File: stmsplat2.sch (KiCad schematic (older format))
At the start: 98 parts, among them J1 C11_2X36, J10 Conn_01x03_Male, J11 Conn_01x02_Male, J12 Conn_01x04_Male, J13 Conn_01x04_Male, J14 Conn_01x02, J15 Conn_01x02, J16 Screw_Terminal_01x03, J17 Screw_Terminal_01x02, J2 C12_2X36, J3 Conn_01x04_Male, J4 Conn_01x04_Male, J5 Conn_Coaxial, J6 Conn_01x04_Male, J7 Conn_01x04_Male, J8 Conn_01x04_Male, J9 Conn_01x03_Male, Q1 BSS138LT1G, U1 ublox_chinese_PCB_module, U10 XCVR_E30-400M20S, U11 3115_module, U2 ESP-C3-13U, U3 SST25VF032B, U4 48L512-48LM01, U5 Opamp_Quad_MCP6024, U6 E180-ZG120A, U7 AZ1084C, U8 MCP6S93-X_UN, U9 DS2485

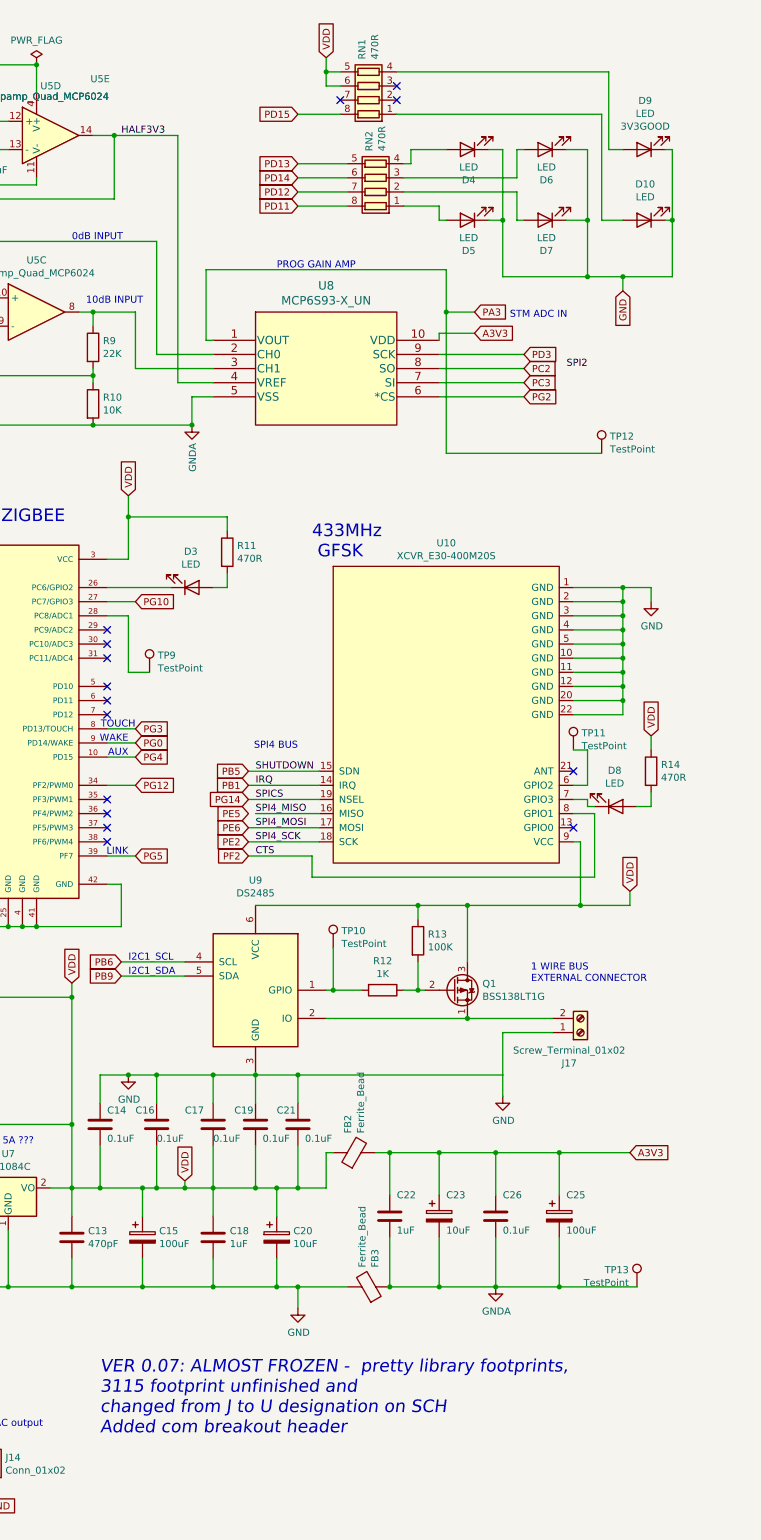
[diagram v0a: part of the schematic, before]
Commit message: Ver 0.9. Initial PCB placement attempt. Some footprints changed
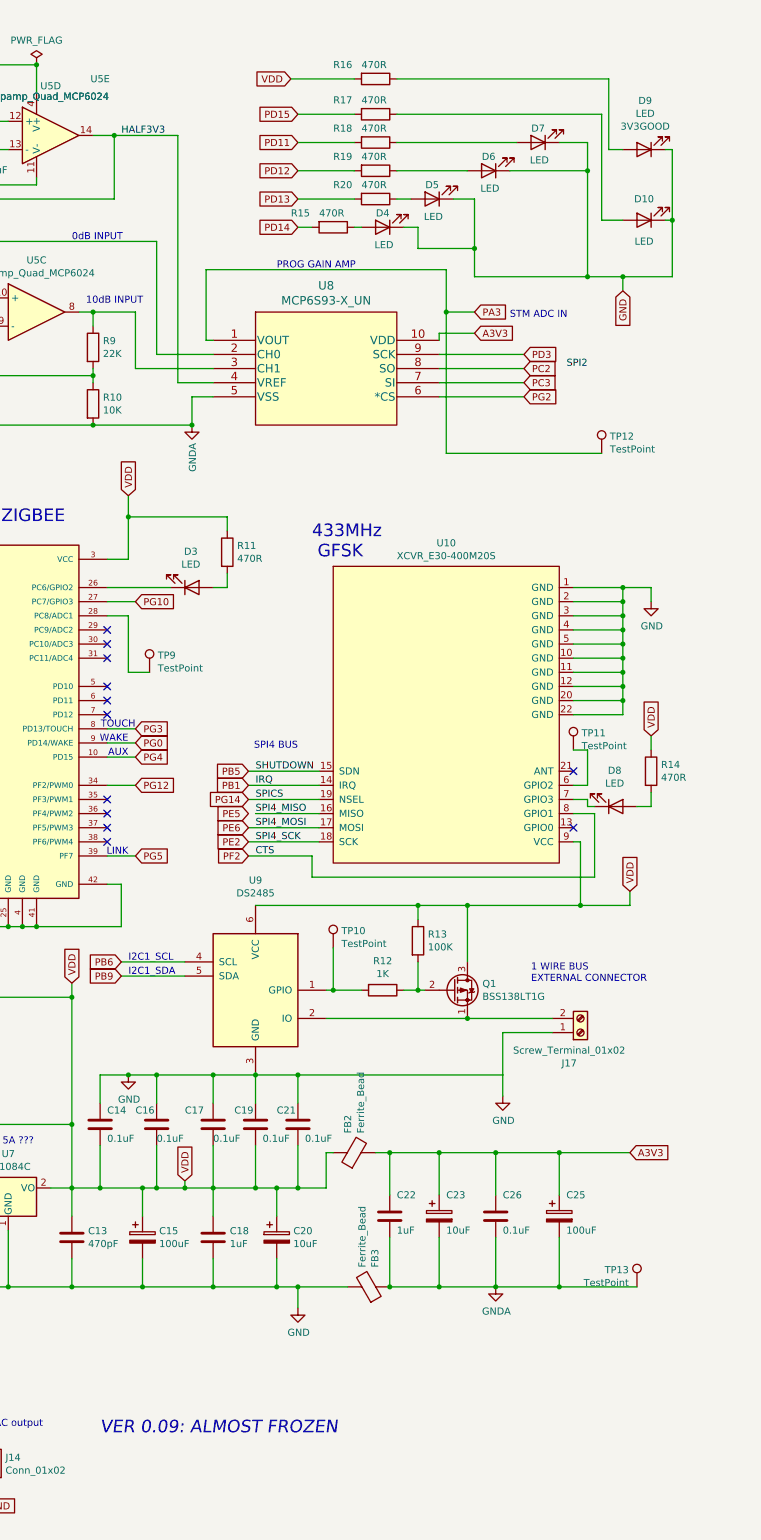
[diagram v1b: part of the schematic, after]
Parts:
- removed RN1, RN2: 470R, Resistor_SMD:R_Array_Convex_4x1206, symbol Device:R_Pack04
- added R15, R16, R17, R18, R19, R20: 470R, Resistor_SMD:R_0805_2012Metric, symbol Device:R
- U3: Alternate (none) -> SST25VF016B (only 2MByte)
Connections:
- net PD11: now also R18.2
- net PD12: now also R19.2
- net PD13: now also R20.2
- net PD14: now also R15.2
- net PD15: now also R17.2
- net VDD: now also R16.2
- net at D7.2 (A): now also R18.1
- net at D5.2 (A): now also R20.1
- net at D6.2 (A): now also R19.1
- net at D4.2 (A): now also R15.1
- net at D9.2 (A): now also R16.1
- net at D10.2 (A): now also R17.1
- no-connect marks 78 -> 75
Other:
- note added: "VER 0.09: ALMOST FROZEN \n"
- note removed: "VER 0.07: ALMOST FROZEN - pretty library footprints,\n3115 footprint unfinished and \nchanged from J to U designation on SCH\nAdded com breakout header"
- moved on the sheet: D4, D5, D6, D7
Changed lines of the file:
@@
 EESchema Schematic File Version 4
-LIBS:stmsplat2-cache
-EELAYER 26 0
+EELAYER 30 0
 EELAYER END
 $Descr A3 16535 11693
@@
 L Device:LED D7
 U 1 1 5BF5D97C
-P 15050 1900
-F 0 "D7" H 15041 2116 50  0000 C CNN
-F 1 "LED" H 15041 2025 50  0000 C CNN
-F 2 "LED_SMD:LED_PLCC-2" H 15050 1900 50  0001 C CNN
-F 3 "~" H 15050 1900 50  0001 C CNN
-	1    15050 1900
+P 15000 1350
+F 0 "D7" H 15000 1250 50  0000 C CNN
+F 1 "LED" H 14991 1475 50  0000 C CNN
+F 2 "LED_SMD:LED_PLCC-2" H 15000 1350 50  0001 C CNN
+F 3 "~" H 15000 1350 50  0001 C CNN
+	1    15000 1350
 	-1   0    0    1
 $EndComp
@@
 L Device:LED D5
 U 1 1 5BF5DD08
-P 14500 1900
-F 0 "D5" H 14491 2116 50  0000 C CNN
-F 1 "LED" H 14491 2025 50  0000 C CNN
-F 2 "LED_SMD:LED_PLCC-2" H 14500 1900 50  0001 C CNN
-F 3 "~" H 14500 1900 50  0001 C CNN
-	1    14500 1900
+P 14250 1750
+F 0 "D5" H 14250 1650 50  0000 C CNN
+F 1 "LED" H 14241 1875 50  0000 C CNN
+F 2 "LED_SMD:LED_PLCC-2" H 14250 1750 50  0001 C CNN
+F 3 "~" H 14250 1750 50  0001 C CNN
+	1    14250 1750
 	-1   0    0    1
 $EndComp
@@
 GND
 $Comp
-L Device:R_Pack04 RN2
-U 1 1 5BF93731
-P 13850 1600
-F 0 "RN2" H 14038 1646 50  0000 L CNN
-F 1 "470R" H 14038 1555 50  0000 L CNN
-F 2 "Resistor_SMD:R_Array_Convex_4x1206" V 14125 1600 50  0001 C CNN
-F 3 "" H 13850 1600 50  0001 C CNN
-	1    13850 1600
-	0    -1   -1   0
-$EndComp
-$Comp
 L Device:LED D6
 U 1 1 5BF93B87
-P 15050 1400
-F 0 "D6" H 15041 1616 50  0000 C CNN
-F 1 "LED" H 15041 1525 50  0000 C CNN
-F 2 "LED_SMD:LED_PLCC-2" H 15050 1400 50  0001 C CNN
-F 3 "~" H 15050 1400 50  0001 C CNN
-	1    15050 1400
+P 14650 1550
+F 0 "D6" H 14650 1450 50  0000 C CNN
+F 1 "LED" H 14641 1675 50  0000 C CNN
+F 2 "LED_SMD:LED_PLCC-2" H 14650 1550 50  0001 C CNN
+F 3 "~" H 14650 1550 50  0001 C CNN
+	1    14650 1550
 	-1   0    0    1
 $EndComp
@@
 L Device:LED D4
 U 1 1 5BF93B8D
-P 14500 1400
-F 0 "D4" H 14491 1616 50  0000 C CNN
-F 1 "LED" H 14491 1525 50  0000 C CNN
-F 2 "LED_SMD:LED_PLCC-2" H 14500 1400 50  0001 C CNN
-F 3 "~" H 14500 1400 50  0001 C CNN
-	1    14500 1400
+P 13900 1950
+F 0 "D4" H 13900 1850 50  0000 C CNN
+F 1 "LED" H 13891 2075 50  0000 C CNN
+F 2 "LED_SMD:LED_PLCC-2" H 13900 1950 50  0001 C CNN
+F 3 "~" H 13900 1950 50  0001 C CNN
+	1    13900 1950
 	-1   0    0    1
 $EndComp
 $Comp
-L Device:R_Pack04 RN1
-U 1 1 5BFA3139
-P 13800 950
-F 0 "RN1" H 13988 996 50  0000 L CNN
-F 1 "470R" H 13988 905 50  0000 L CNN
-F 2 "Resistor_SMD:R_Array_Convex_4x1206" V 14075 950 50  0001 C CNN
-F 3 "" H 13800 950 50  0001 C CNN
-	1    13800 950
-	0    -1   -1   0
-$EndComp
-$Comp
 L Device:LED D10
 U 1 1 5BFA313F
 P 15750 1900
-F 0 "D10" H 15742 1645 50  0000 C CNN
-F 1 "LED" H 15742 1736 50  0000 C CNN
+F 0 "D10" H 15750 1750 50  0000 C CNN
+F 1 "LED" H 15750 2050 50  0000 C CNN
 F 2 "LED_SMD:LED_PLCC-2" H 15750 1900 50  0001 C CNN
 F 3 "~" H 15750 1900 50  0001 C CNN
@@
 	-1   0    0    1
 $EndComp
-Wire Wire Line
-	14650 1400 14750 1400
-Wire Wire Line
-	14750 1400 14750 1900
-Wire Wire Line
-	15350 2300 15350 1900
-Wire Wire Line
-	15350 1400 15200 1400
-Wire Wire Line
-	15200 1900 15350 1900
-Connection ~ 15350 1900
-Wire Wire Line
-	15350 1900 15350 1400
-Wire Wire Line
-	14650 1900 14750 1900
-Connection ~ 14750 1900
-Wire Wire Line
-	14750 1900 14750 2300
-Wire Wire Line
-	14350 1400 14100 1400
-Wire Wire Line
-	14100 1400 14100 1500
-Wire Wire Line
-	14100 1500 14050 1500
-Wire Wire Line
-	14050 1600 14850 1600
-Wire Wire Line
-	14850 1600 14850 1400
-Wire Wire Line
-	14850 1400 14900 1400
-Wire Wire Line
-	14050 1700 14850 1700
-Wire Wire Line
-	14850 1700 14850 1900
-Wire Wire Line
-	14850 1900 14900 1900
-Wire Wire Line
-	14350 1900 14300 1900
-Wire Wire Line
-	14300 1900 14300 1800
-Wire Wire Line
-	14300 1800 14050 1800
 Text GLabel 15600 2400 3    50   Input ~ 0
 GND
 Wire Wire Line
-	15500 1400 15500 850
-Wire Wire Line
-	15500 850  14000 850
+	15500 1400 15500 900
 Wire Wire Line
 	15600 1900 15450 1900
-Wire Wire Line
-	14750 2300 15350 2300
 Connection ~ 15350 2300
 Wire Wire Line
@@
 Wire Wire Line
 	15600 2300 15350 2300
-Wire Wire Line
-	13600 850  13500 850
-Wire Wire Line
-	13500 850  13500 750
-Text GLabel 13500 750  1    50   Input ~ 0
+Text GLabel 13250 900  0    50   Input ~ 0
 VDD
 $Comp
@@
 Text Label 7050 10300 0    50   ~ 0
 NXT_RX
-Wire Wire Line
-	13600 1150 13300 1150
-Wire Wire Line
-	13650 1700 13300 1700
-Wire Wire Line
-	13650 1800 13300 1800
 Text GLabel 13300 1150 0    50   Input ~ 0
 PD15
-Text GLabel 13300 1600 0    50   Input ~ 0
+Text GLabel 13300 1950 0    50   Input ~ 0
 PD14
-Text GLabel 13300 1500 0    50   Input ~ 0
+Text GLabel 13300 1750 0    50   Input ~ 0
 PD13
-Text GLabel 13300 1700 0    50   Input ~ 0
+Text GLabel 13300 1550 0    50   Input ~ 0
 PD12
-Text GLabel 13300 1800 0    50   Input ~ 0
+Text GLabel 13300 1350 0    50   Input ~ 0
 PD11
 $Comp
@@
 PA3
 Wire Wire Line
-	13300 1500 13650 1500
-Wire Wire Line
-	13300 1600 13650 1600
-Wire Wire Line
 	14300 2850 14900 2850
 Wire Wire Line
@@
 F 3 "" H 6200 4100 50  0001 L BNN
 F 4 "Microchip" H 6200 4100 50  0001 L BNN "MANUFACTURER"
+F 5 "SST25VF016B (only 2MByte)" H 6200 4100 50  0001 C CNN "Alternate"
 	1    6200 4100
 	-1   0    0    -1
@@
 	5800 10600 5800 10900
 Wire Wire Line
-	13500 850  13500 950
-Wire Wire Line
-	13500 950  13600 950
-Connection ~ 13500 850
-Wire Wire Line
 	5800 2650 5950 2650
 Wire Wire Line
@@
 SERIAL FLASH ROM\n  AND NVRAM
 Text Notes 11900 10500 0    89   Italic 0
-VER 0.07: ALMOST FROZEN -  pretty library footprints,\n3115 footprint unfinished and \nchanged from J to U designation on SCH\nAdded com breakout header
+VER 0.09: ALMOST FROZEN \n
 $Comp
 L Connector_Generic:Conn_01x02 J14
@@
 NoConn ~ 15250 6200
 NoConn ~ 15250 5800
-NoConn ~ 14000 950
 Text Label 3000 1200 0    50   ~ 0
 PC5
@@
 Text Label 3000 2800 0    50   ~ 0
 PF4
-NoConn ~ 14000 1050
 NoConn ~ 6650 6700
 NoConn ~ 2500 2700
-NoConn ~ 13600 1050
 $Comp
 L power:GNDA #PWR0105
@@
 Text Label 9300 8150 2    50   ~ 0
 RAWGND
+$Comp
+L Device:R R16
+U 1 1 61E89584
+P 13850 900
+F 0 "R16" V 13750 600 50  0000 L CNN
+F 1 "470R" V 13750 800 50  0000 L CNN
+F 2 "Resistor_SMD:R_0805_2012Metric" V 13780 900 50  0001 C CNN
+F 3 "~" H 13850 900 50  0001 C CNN
+	1    13850 900
+	0    1    1    0
+$EndComp
+$Comp
+L Device:R R17
+U 1 1 61E89DEC
+P 13850 1150
+F 0 "R17" V 13750 850 50  0000 L CNN
+F 1 "470R" V 13750 1050 50  0000 L CNN
+F 2 "Resistor_SMD:R_0805_2012Metric" V 13780 1150 50  0001 C CNN
+F 3 "~" H 13850 1150 50  0001 C CNN
+	1    13850 1150
+	0    1    1    0
+$EndComp
+Wire Wire Line
+	14400 1750 14550 1750
+Wire Wire Line
+	14550 2300 15350 2300
+Wire Wire Line
+	14050 1950 14150 1950
+Wire Wire Line
+	14150 1950 14150 2100
+Wire Wire Line
+	14150 2100 14550 2100
+Wire Wire Line
+	14550 1750 14550 2100
+Connection ~ 14550 2100
+Wire Wire Line
+	14550 2100 14550 2300
+Wire Wire Line
+	13300 1150 13700 1150
+$Comp
+L Device:R R18
+U 1 1 6280AE2A
+P 13850 1350
+F 0 "R18" V 13750 1050 50  0000 L CNN
+F 1 "470R" V 13750 1250 50  0000 L CNN
+F 2 "Resistor_SMD:R_0805_2012Metric" V 13780 1350 50  0001 C CNN
+F 3 "~" H 13850 1350 50  0001 C CNN
+	1    13850 1350
+	0    1    1    0
+$EndComp
+$Comp
+L Device:R R19
+U 1 1 6280AF10
+P 13850 1550
+F 0 "R19" V 13750 1250 50  0000 L CNN
+F 1 "470R" V 13750 1450 50  0000 L CNN
+F 2 "Resistor_SMD:R_0805_2012Metric" V 13780 1550 50  0001 C CNN
+F 3 "~" H 13850 1550 50  0001 C CNN
+	1    13850 1550
+	0    1    1    0
+$EndComp
+$Comp
+L Device:R R20
+U 1 1 6280AFF4
+P 13850 1750
+F 0 "R20" V 13750 1450 50  0000 L CNN
+F 1 "470R" V 13750 1650 50  0000 L CNN
+F 2 "Resistor_SMD:R_0805_2012Metric" V 13780 1750 50  0001 C CNN
+F 3 "~" H 13850 1750 50  0001 C CNN
+	1    13850 1750
+	0    1    1    0
+$EndComp
+$Comp
+L Device:R R15
+U 1 1 6280B0DA
+P 13550 1950
+F 0 "R15" V 13450 1650 50  0000 L CNN
+F 1 "470R" V 13450 1850 50  0000 L CNN
+F 2 "Resistor_SMD:R_0805_2012Metric" V 13480 1950 50  0001 C CNN
+F 3 "~" H 13550 1950 50  0001 C CNN
+	1    13550 1950
+	0    1    1    0
+$EndComp
+Wire Wire Line
+	13300 1350 13700 1350
+Wire Wire Line
+	13300 1550 13700 1550
+Wire Wire Line
+	13300 1750 13700 1750
+Wire Wire Line
+	13300 1950 13400 1950
+Wire Wire Line
+	13700 1950 13750 1950
+Wire Wire Line
+	14000 1750 14100 1750
+Wire Wire Line
+	14000 1350 14850 1350
+Wire Wire Line
+	14000 1550 14500 1550
+Wire Wire Line
+	14800 1550 15350 1550
+Connection ~ 15350 1550
+Wire Wire Line
+	15350 1550 15350 2300
+Wire Wire Line
+	15150 1350 15350 1350
+Wire Wire Line
+	15350 1350 15350 1550
+Wire Wire Line
+	13250 900  13700 900
+Wire Wire Line
+	14000 900  15500 900
 $EndSCHEMATC
